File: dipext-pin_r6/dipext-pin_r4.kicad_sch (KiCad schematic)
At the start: 20 parts, among them J1 ZIF, J2 IDC40, J3 Conn_02x20_Odd_Even, J4 Conn_02x20_Odd_Even, J5 01x20, J6 01x20, J7 01x20, J8 01x20

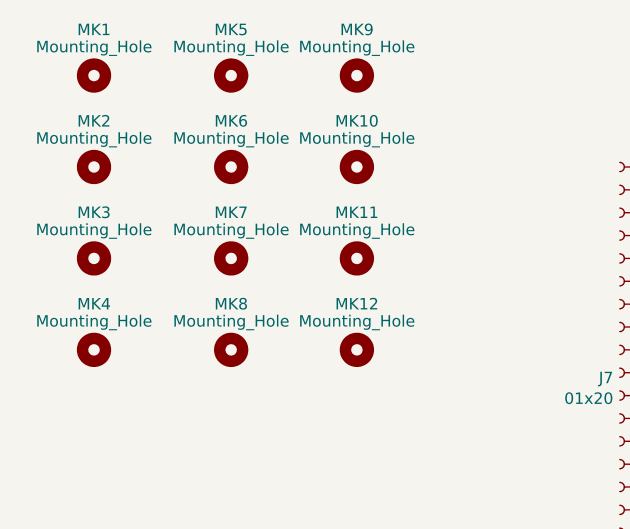
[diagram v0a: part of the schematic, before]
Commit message: dipext-pin_r6: simplify mounting holes
Signed-off-by: John McMaster <johndmcmaster@gmail.com>
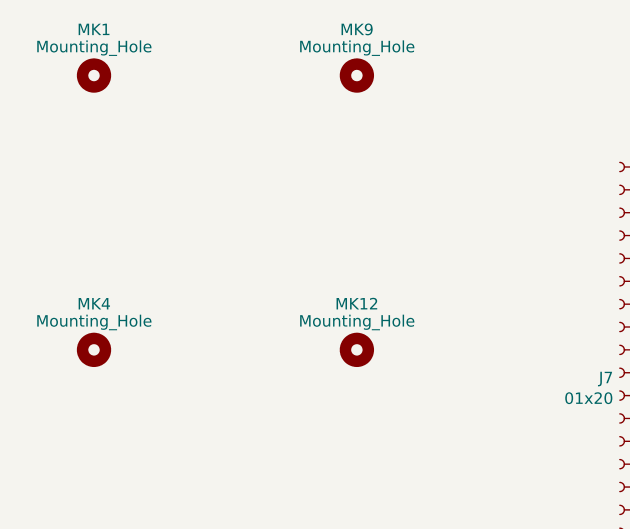
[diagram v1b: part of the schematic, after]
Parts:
- removed MK10, MK11, MK2, MK3, MK5, MK6, MK7, MK8: Mounting_Hole, Mounting_Holes:MountingHole_8.4mm_M8, symbol dipext-pin_r4-rescue:Mounting_Hole
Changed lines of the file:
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@@
-    )
-  )
-  (symbol (lib_id "dipext-pin_r4-rescue:Mounting_Hole") (at 30.48 45.72 0) (unit 1)
-    (in_bom yes) (on_board yes)
-    (property "Reference" "MK2" (id 0) (at 30.48 40.64 0))
-    (property "Value" "Mounting_Hole" (id 1) (at 30.48 42.545 0))
-    (property "Footprint" "Mounting_Holes:MountingHole_8.4mm_M8" (id 2) (at 30.48 45.72 0)
-      (effects (font (size 1.27 1.27)) hide)
-    )
-    (property "Datasheet" "" (id 3) (at 30.48 45.72 0)
-      (effects (font (size 1.27 1.27)) hide)
-    )
-  )
-  (symbol (lib_id "dipext-pin_r4-rescue:Mounting_Hole") (at 30.48 55.88 0) (unit 1)
-    (in_bom yes) (on_board yes)
-    (property "Reference" "MK3" (id 0) (at 30.48 50.8 0))
-    (property "Value" "Mounting_Hole" (id 1) (at 30.48 52.705 0))
-    (property "Footprint" "Mounting_Holes:MountingHole_8.4mm_M8" (id 2) (at 30.48 55.88 0)
-      (effects (font (size 1.27 1.27)) hide)
-    )
-    (property "Datasheet" "" (id 3) (at 30.48 55.88 0)
-      (effects (font (size 1.27 1.27)) hide)
     )
   )
@@
     )
   )
-  (symbol (lib_id "dipext-pin_r4-rescue:Mounting_Hole") (at 45.72 35.56 0) (unit 1)
-    (in_bom yes) (on_board yes)
-    (property "Reference" "MK5" (id 0) (at 45.72 30.48 0))
-    (property "Value" "Mounting_Hole" (id 1) (at 45.72 32.385 0))
-    (property "Footprint" "Mounting_Holes:MountingHole_8.4mm_M8" (id 2) (at 45.72 35.56 0)
-      (effects (font (size 1.27 1.27)) hide)
-    )
-    (property "Datasheet" "" (id 3) (at 45.72 35.56 0)
-      (effects (font (size 1.27 1.27)) hide)
-    )
-  )
-  (symbol (lib_id "dipext-pin_r4-rescue:Mounting_Hole") (at 45.72 45.72 0) (unit 1)
-    (in_bom yes) (on_board yes)
-    (property "Reference" "MK6" (id 0) (at 45.72 40.64 0))
-    (property "Value" "Mounting_Hole" (id 1) (at 45.72 42.545 0))
-    (property "Footprint" "Mounting_Holes:MountingHole_8.4mm_M8" (id 2) (at 45.72 45.72 0)
-      (effects (font (size 1.27 1.27)) hide)
-    )
-    (property "Datasheet" "" (id 3) (at 45.72 45.72 0)
-      (effects (font (size 1.27 1.27)) hide)
-    )
-  )
-  (symbol (lib_id "dipext-pin_r4-rescue:Mounting_Hole") (at 45.72 55.88 0) (unit 1)
-    (in_bom yes) (on_board yes)
-    (property "Reference" "MK7" (id 0) (at 45.72 50.8 0))
-    (property "Value" "Mounting_Hole" (id 1) (at 45.72 52.705 0))
-    (property "Footprint" "Mounting_Holes:MountingHole_8.4mm_M8" (id 2) (at 45.72 55.88 0)
-      (effects (font (size 1.27 1.27)) hide)
-    )
-    (property "Datasheet" "" (id 3) (at 45.72 55.88 0)
-      (effects (font (size 1.27 1.27)) hide)
-    )
-  )
-  (symbol (lib_id "dipext-pin_r4-rescue:Mounting_Hole") (at 45.72 66.04 0) (unit 1)
-    (in_bom yes) (on_board yes)
-    (property "Reference" "MK8" (id 0) (at 45.72 60.96 0))
-    (property "Value" "Mounting_Hole" (id 1) (at 45.72 62.865 0))
-    (property "Footprint" "Mounting_Holes:MountingHole_8.4mm_M8" (id 2) (at 45.72 66.04 0)
-      (effects (font (size 1.27 1.27)) hide)
-    )
-    (property "Datasheet" "" (id 3) (at 45.72 66.04 0)
-      (effects (font (size 1.27 1.27)) hide)
-    )
-  )
   (symbol (lib_id "dipext-pin_r4-rescue:Mounting_Hole") (at 59.69 35.56 0) (unit 1)
     (in_bom yes) (on_board yes)
@@
     )
     (property "Datasheet" "" (id 3) (at 59.69 35.56 0)
-      (effects (font (size 1.27 1.27)) hide)
-    )
-  )
-  (symbol (lib_id "dipext-pin_r4-rescue:Mounting_Hole") (at 59.69 45.72 0) (unit 1)
-    (in_bom yes) (on_board yes)
-    (property "Reference" "MK10" (id 0) (at 59.69 40.64 0))
-    (property "Value" "Mounting_Hole" (id 1) (at 59.69 42.545 0))
-    (property "Footprint" "Mounting_Holes:MountingHole_8.4mm_M8" (id 2) (at 59.69 45.72 0)
-      (effects (font (size 1.27 1.27)) hide)
-    )
-    (property "Datasheet" "" (id 3) (at 59.69 45.72 0)
-      (effects (font (size 1.27 1.27)) hide)
-    )
-  )
-  (symbol (lib_id "dipext-pin_r4-rescue:Mounting_Hole") (at 59.69 55.88 0) (unit 1)
-    (in_bom yes) (on_board yes)
-    (property "Reference" "MK11" (id 0) (at 59.69 50.8 0))
-    (property "Value" "Mounting_Hole" (id 1) (at 59.69 52.705 0))
-    (property "Footprint" "Mounting_Holes:MountingHole_8.4mm_M8" (id 2) (at 59.69 55.88 0)
-      (effects (font (size 1.27 1.27)) hide)
-    )
-    (property "Datasheet" "" (id 3) (at 59.69 55.88 0)
       (effects (font (size 1.27 1.27)) hide)
     )
@@
       (reference "MK1") (unit 1) (value "Mounting_Hole") (footprint "Mounting_Holes:MountingHole_8.4mm_M8")
     )
-    (path "/00000000-0000-0000-0000-00005b739211"
-      (reference "MK2") (unit 1) (value "Mounting_Hole") (footprint "Mounting_Holes:MountingHole_8.4mm_M8")
-    )
-    (path "/00000000-0000-0000-0000-00005b739245"
-      (reference "MK3") (unit 1) (value "Mounting_Hole") (footprint "Mounting_Holes:MountingHole_8.4mm_M8")
-    )
     (path "/00000000-0000-0000-0000-00005b739268"
       (reference "MK4") (unit 1) (value "Mounting_Hole") (footprint "Mounting_Holes:MountingHole_8.4mm_M8")
     )
-    (path "/00000000-0000-0000-0000-00005b73a514"
-      (reference "MK5") (unit 1) (value "Mounting_Hole") (footprint "Mounting_Holes:MountingHole_8.4mm_M8")
-    )
-    (path "/00000000-0000-0000-0000-00005b73a51a"
-      (reference "MK6") (unit 1) (value "Mounting_Hole") (footprint "Mounting_Holes:MountingHole_8.4mm_M8")
-    )
-    (path "/00000000-0000-0000-0000-00005b73a520"
-      (reference "MK7") (unit 1) (value "Mounting_Hole") (footprint "Mounting_Holes:MountingHole_8.4mm_M8")
-    )
-    (path "/00000000-0000-0000-0000-00005b73a526"
-      (reference "MK8") (unit 1) (value "Mounting_Hole") (footprint "Mounting_Holes:MountingHole_8.4mm_M8")
-    )
     (path "/00000000-0000-0000-0000-00005b73a7ca"
       (reference "MK9") (unit 1) (value "Mounting_Hole") (footprint "Mounting_Holes:MountingHole_8.4mm_M8")
     )
-    (path "/00000000-0000-0000-0000-00005b73a7d0"
-      (reference "MK10") (unit 1) (value "Mounting_Hole") (footprint "Mounting_Holes:MountingHole_8.4mm_M8")
-    )
-    (path "/00000000-0000-0000-0000-00005b73a7d6"
-      (reference "MK11") (unit 1) (value "Mounting_Hole") (footprint "Mounting_Holes:MountingHole_8.4mm_M8")
-    )
     (path "/00000000-0000-0000-0000-00005b73a7dc"
